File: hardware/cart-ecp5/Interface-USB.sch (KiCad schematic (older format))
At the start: 41 parts, among them J5 USB_C_USB2.0, U10 93C46BT-I_OT, U11 FT2232HQ, U3 USBLC6-2SC6, X2 DSC60xx

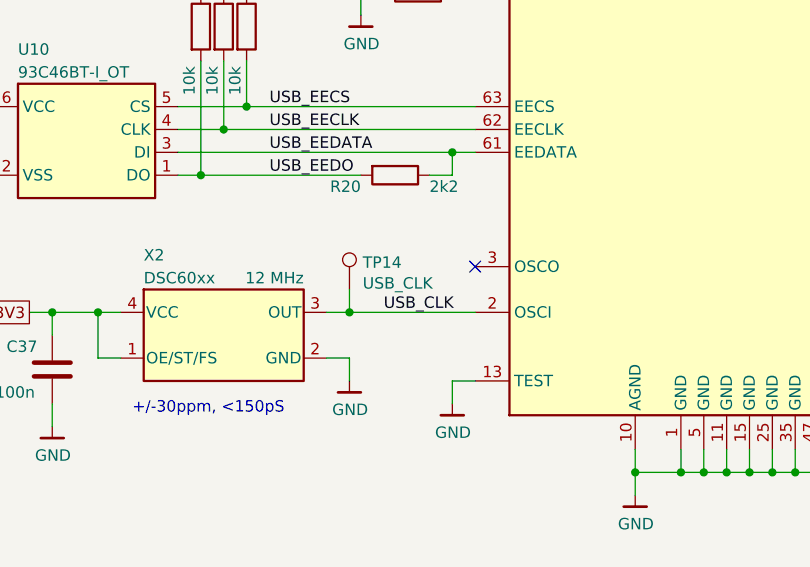
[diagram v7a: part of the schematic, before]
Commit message: Don't stuff the net name into test point values
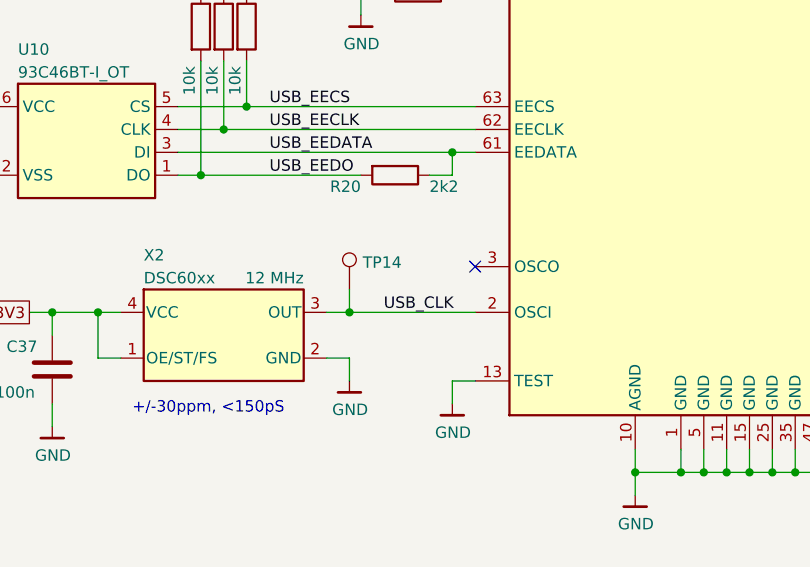
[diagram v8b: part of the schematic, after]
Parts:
- TP14: value USB_CLK -> TestPoint
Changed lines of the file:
@@
 AR Path="/5F4552C5/5FE0424B" Ref="TP14"  Part="1"
 F 0 "TP14" H 10058 7218 50  0000 L CNN
-F 1 "USB_CLK" H 10058 7127 50  0000 L CNN
+F 1 "TestPoint" H 10058 7127 50  0001 L CNN
 F 2 "ng_test:TestPoint_Pad_D0.5mm" H 10200 7100 50  0001 C CNN
 F 3 "~" H 10200 7100 50  0001 C CNN
